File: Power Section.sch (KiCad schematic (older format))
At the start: 55 parts, among them J17 CK-JS102011SAQN, J4 USB_C_Receptacle_USB2.0, Q1 SSM6J507NU, Q2 SSM6J507NU, Q3 SSM6J507NU, U1 LM1117LDX, U2 LDFM33PVR, U5 MCP73213, U6 ETA3000, U7 STUSB4500QTR

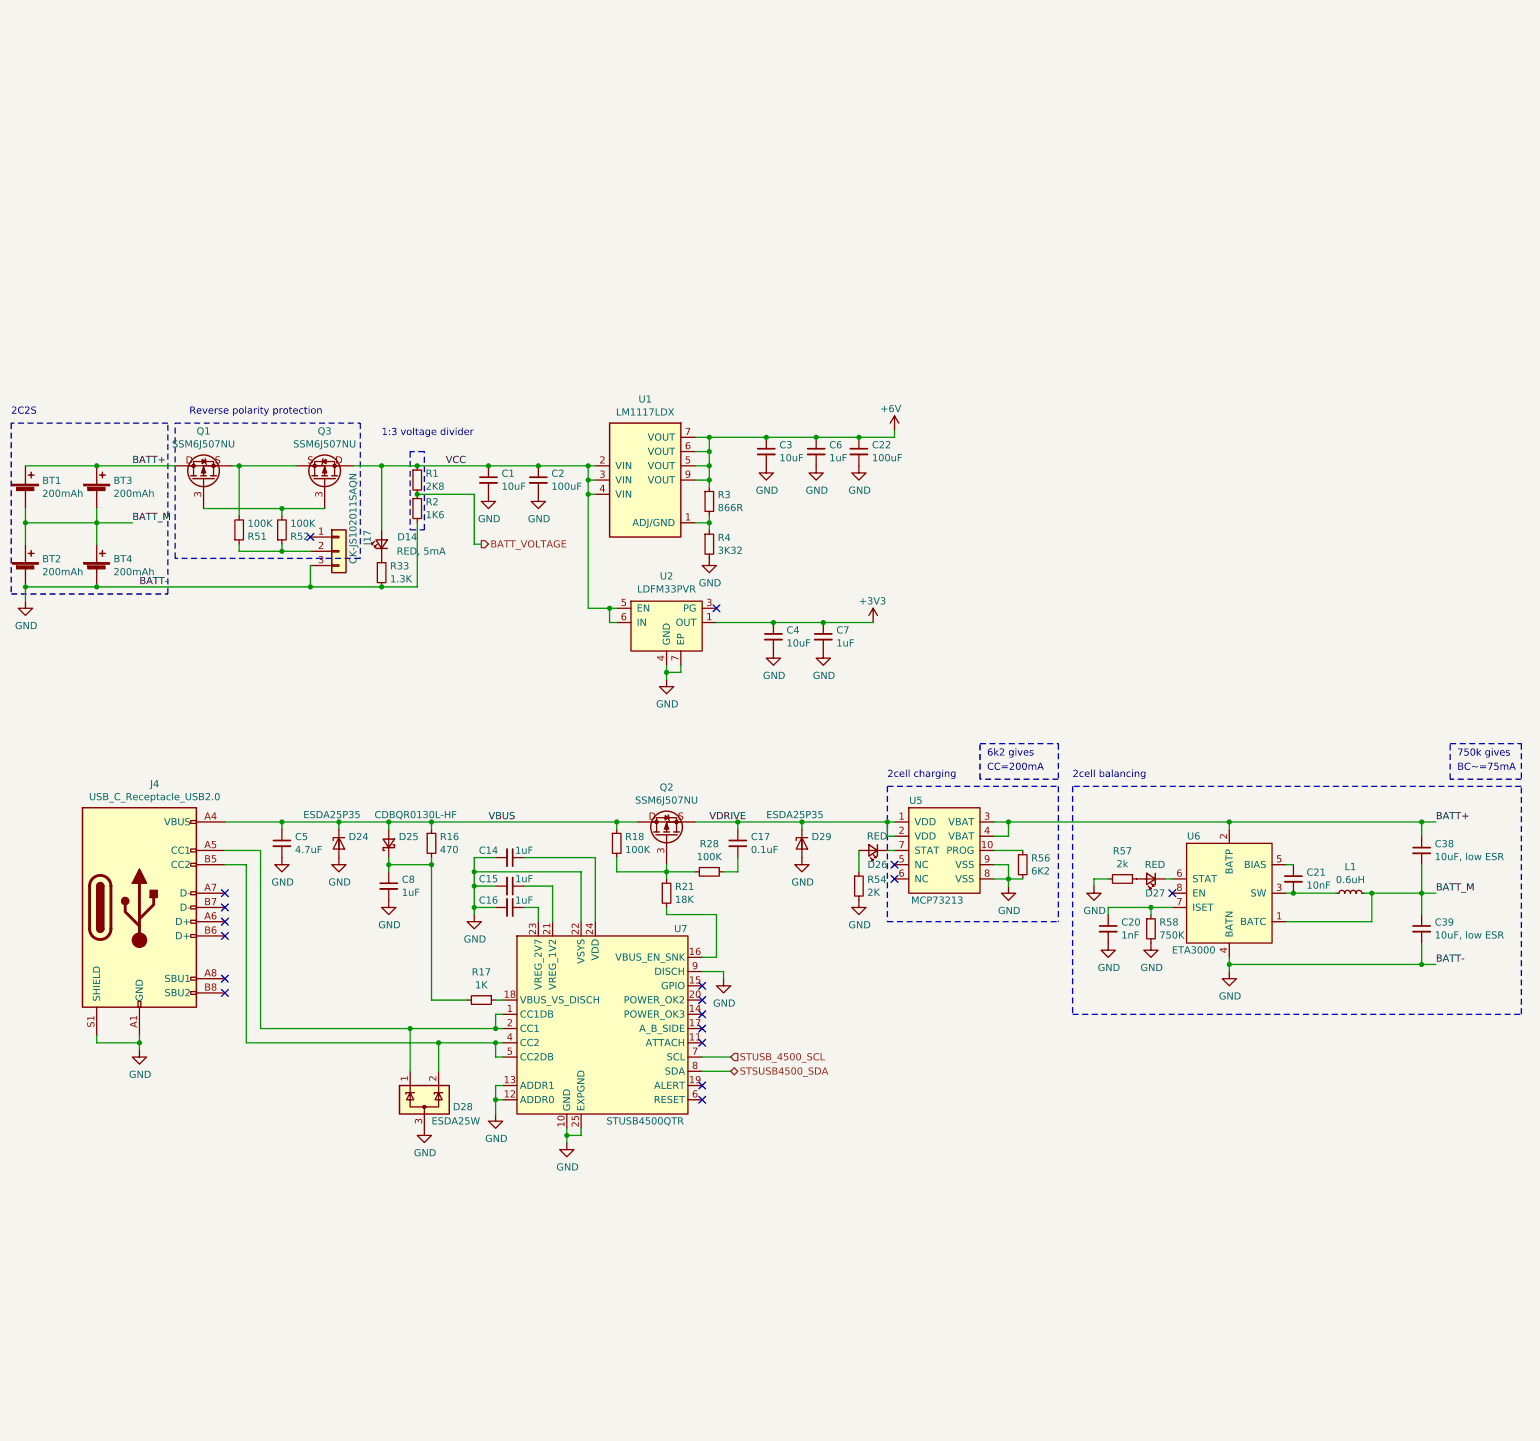
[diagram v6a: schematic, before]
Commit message: Dodano możliwość zasilania (nie tylko ładowania)  myszki z usb-c
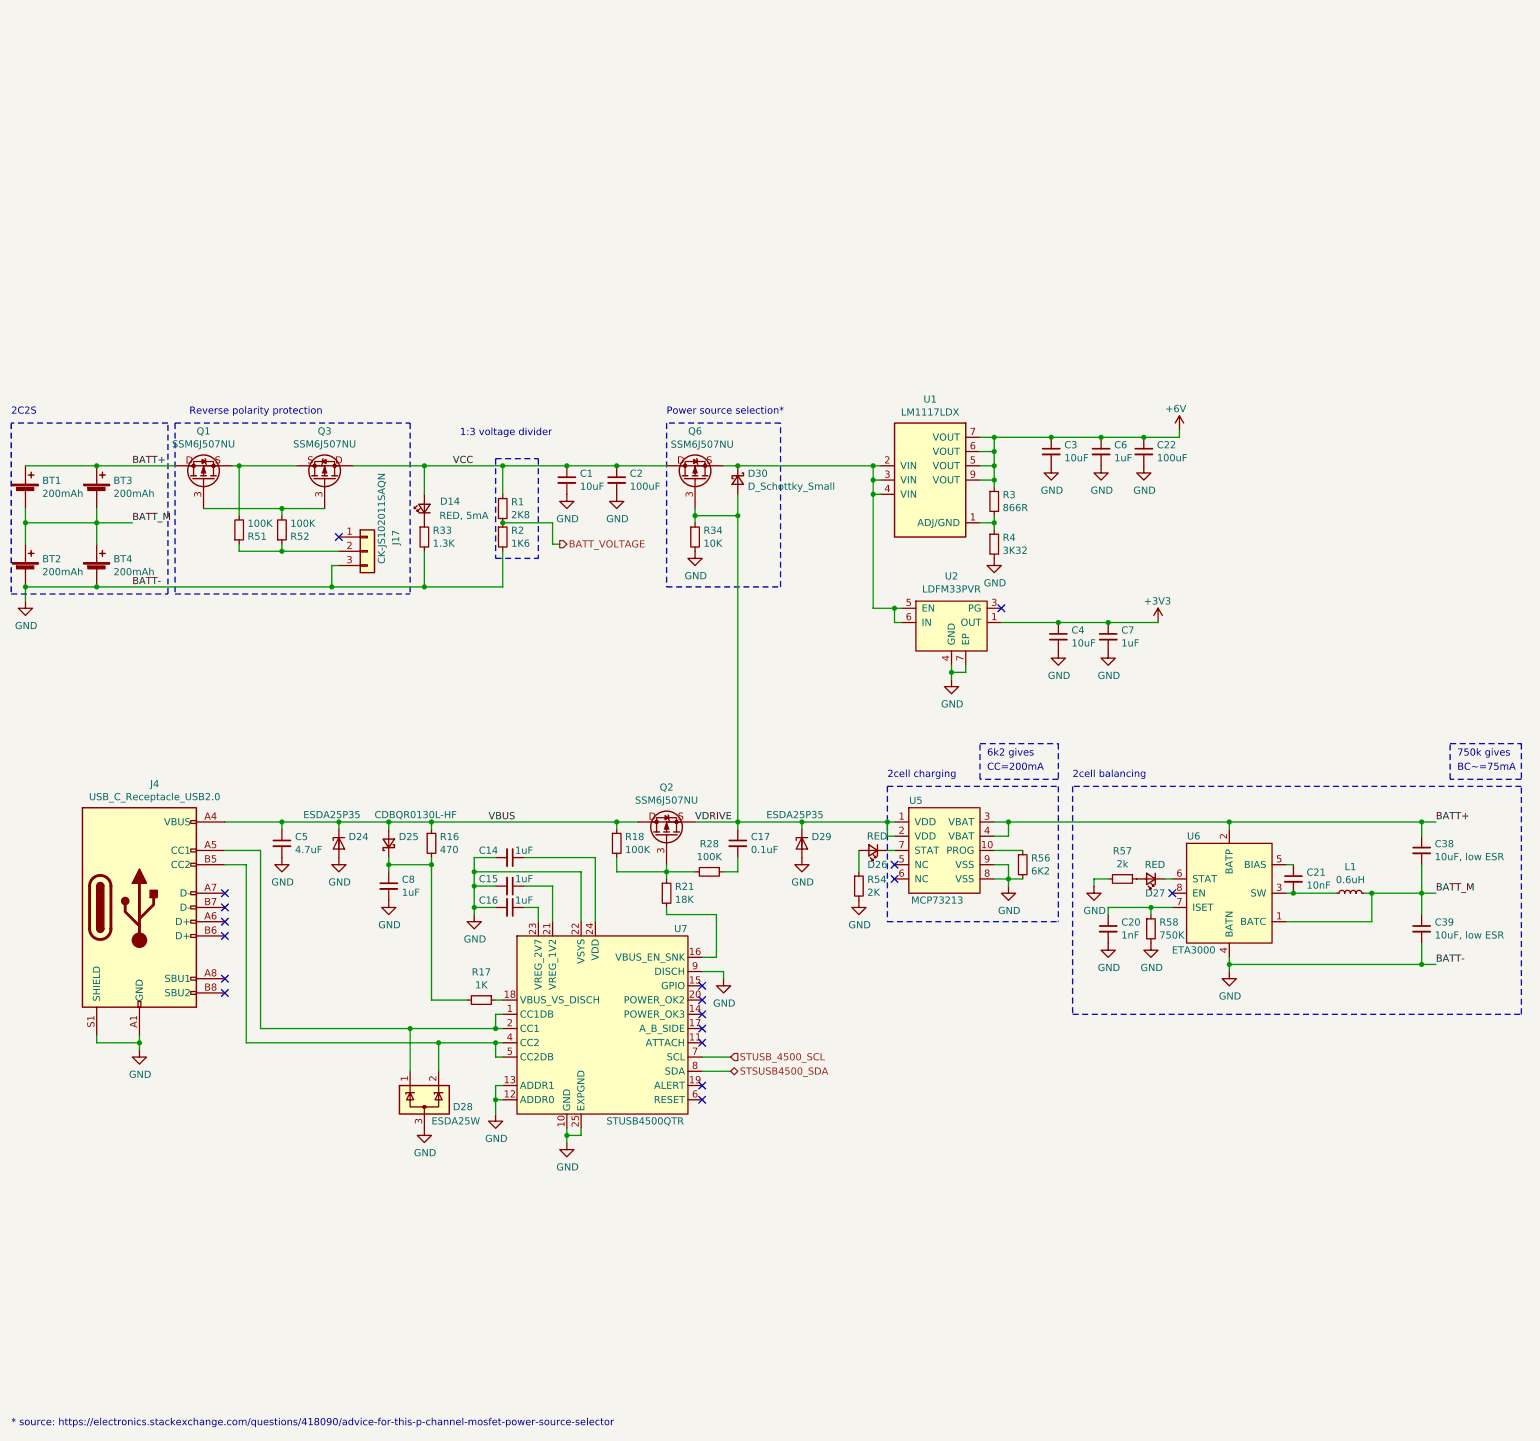
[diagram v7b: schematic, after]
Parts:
- added D30: D_Schottky_Small, symbol Device:D_Schottky_Small
- added Q6: SSM6J507NU, footprints:UDFN6B, symbol synermycha-electronics:SSM6J507NU
- added R34: 10K, Resistor_SMD:R_0402_1005Metric, symbol Device:R_Small
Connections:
- net GND: now also R34.2
- net VCC: now also Q6.1 (D), Q6.2 (D), Q6.5 (D), Q6.6 (D), Q6.D; no longer U1.2 (VIN), U1.3 (VIN), U1.4 (VIN), U2.5 (EN), U2.6 (IN)
- net VDRIVE: now also D30.2 (A), Q6.3 (G), R34.1
- new net: D30.1 (K), Q6.4 (S), Q6.S, U1.2 (VIN), U1.3 (VIN), U1.4 (VIN), U2.5 (EN), U2.6 (IN)
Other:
- note added: "* source: https://electronics.stackexchange.com/questions/418090/advice-for-this-p-channel-mosfet-power-source-selector"
- note added: "Power source selection*"
- moved on the sheet: C1, C2, C22, C3, C4, C6, C7, D14, J17, R1, R2, R3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

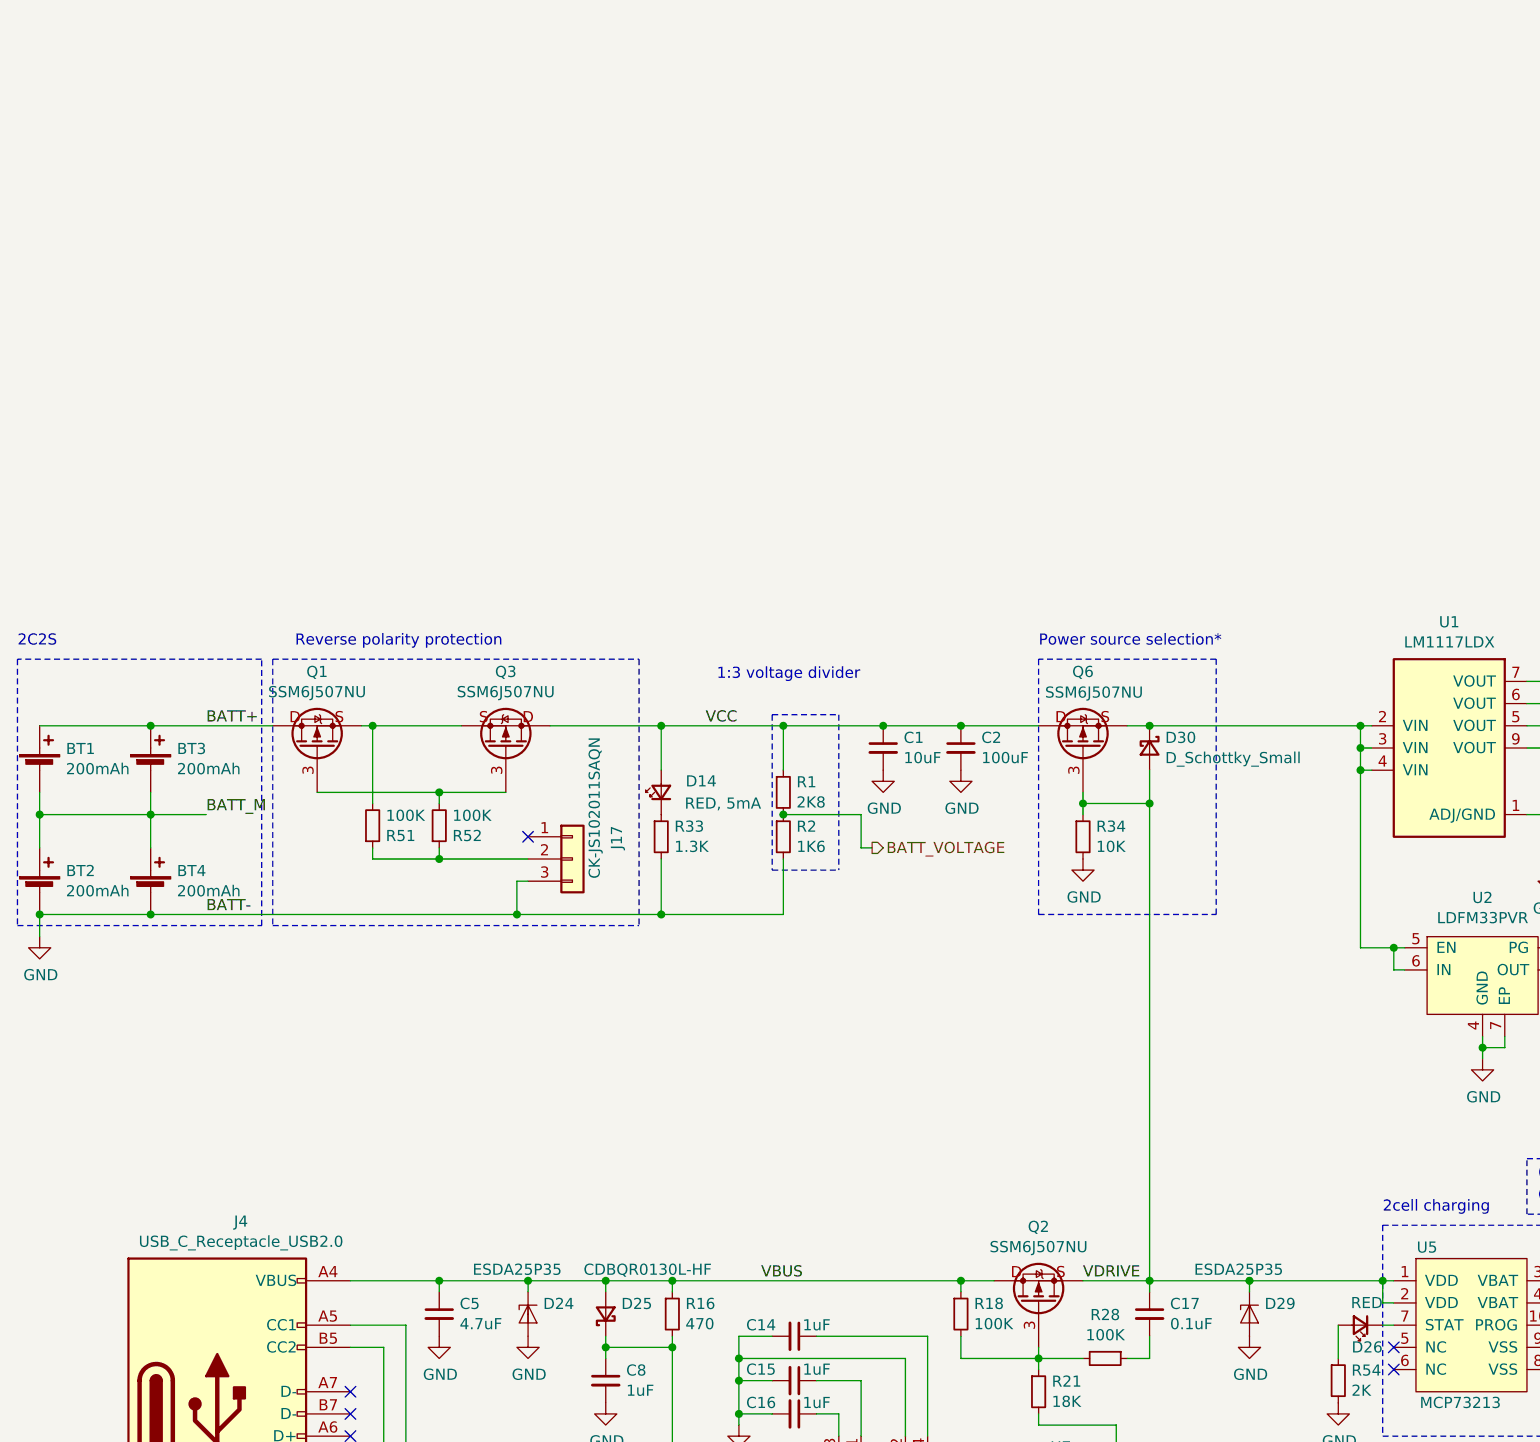
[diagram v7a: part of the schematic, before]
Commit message: Myszka może być wyłączona także podczas zasilania z USB. Zmiany na PCB
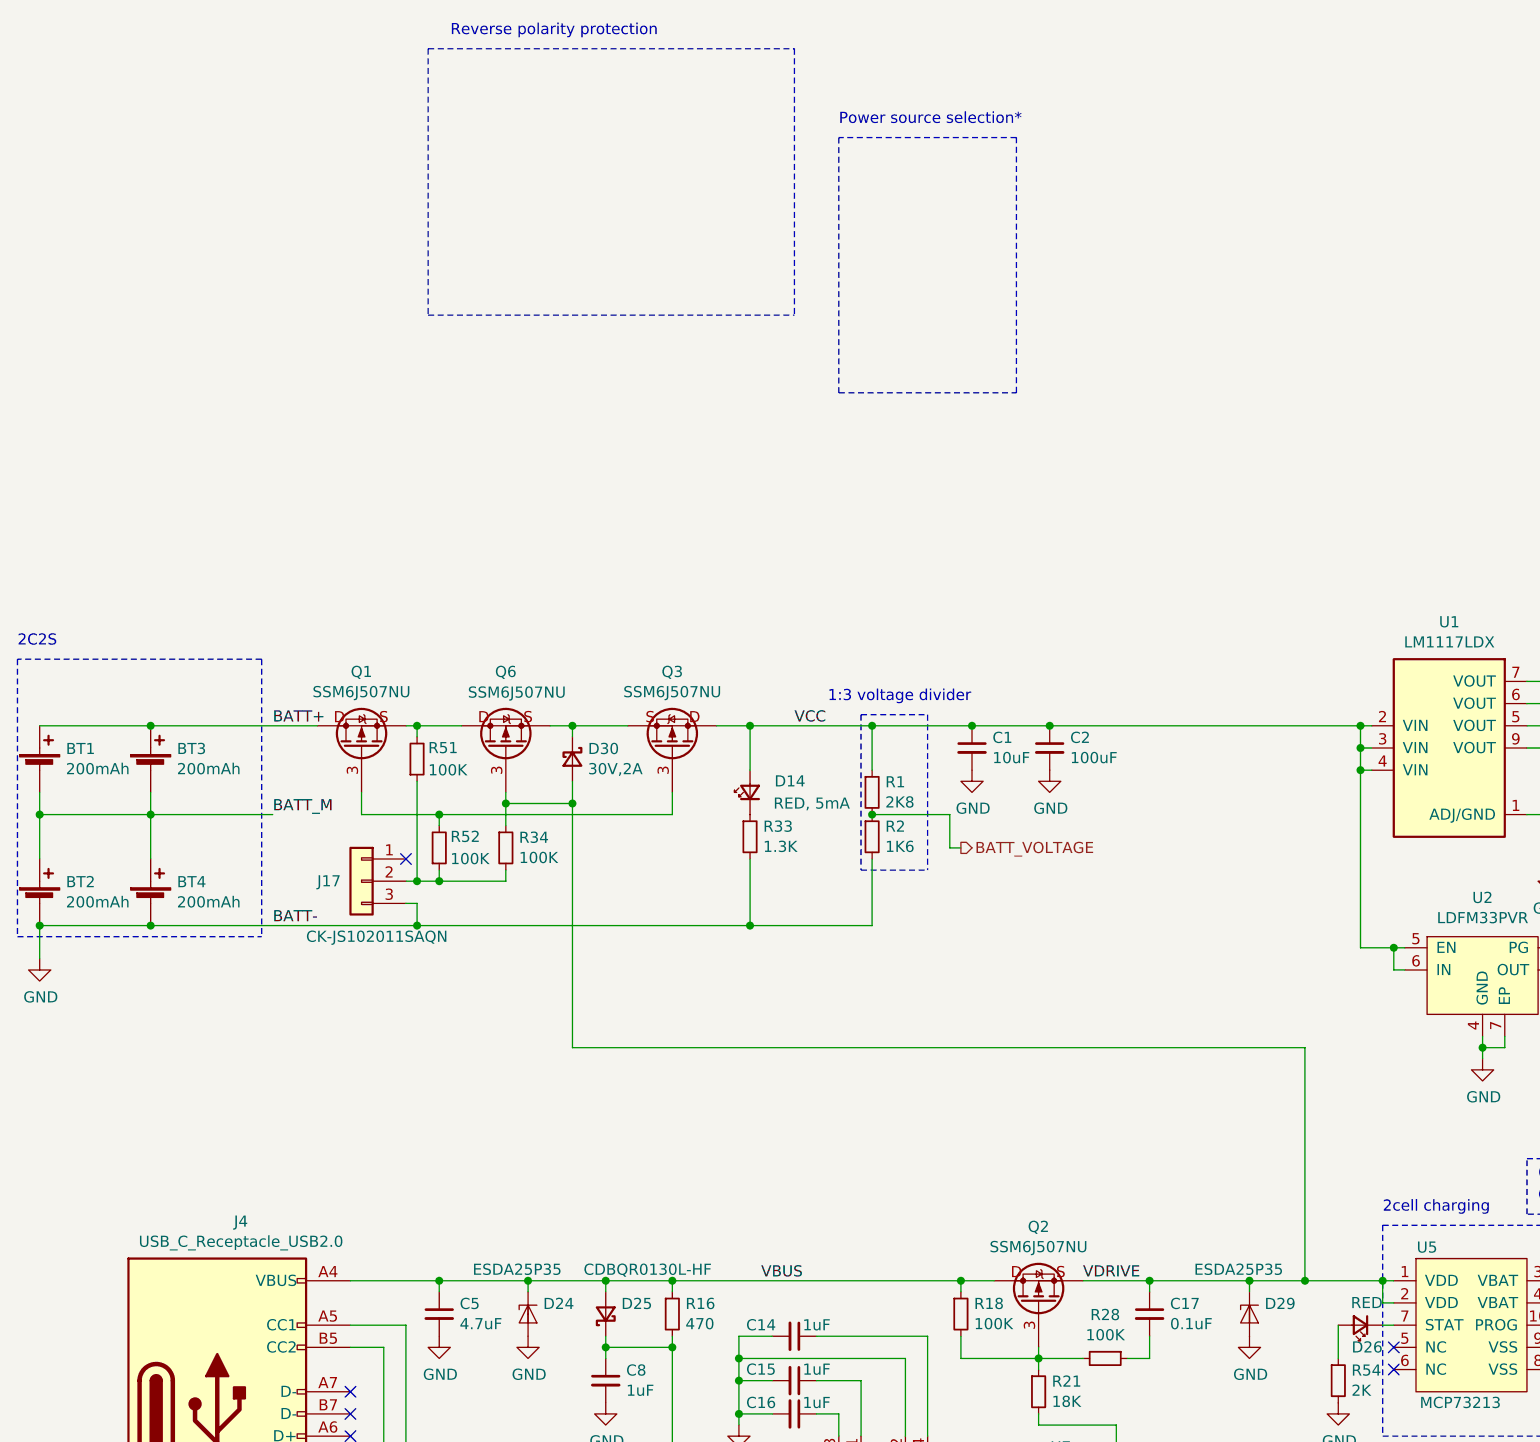
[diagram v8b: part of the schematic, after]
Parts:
- D30: value D_Schottky_Small -> 30V,2A; footprint (none) -> Diode_SMD:D_SOD-123F
- R34: value 10K -> 100K
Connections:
- net GND: no longer R34.2
- net VCC: now also U1.2 (VIN), U1.3 (VIN), U1.4 (VIN), U2.5 (EN), U2.6 (IN); no longer Q6.1 (D), Q6.2 (D), Q6.5 (D), Q6.6 (D), Q6.D
- net at J17.2 (Pin_2), R51.1, R52.1: now also R34.2
- net at Q1.4 (S), Q1.S, R51.2: now also Q6.1 (D), Q6.2 (D), Q6.5 (D), Q6.6 (D), Q6.D; no longer Q3.4 (S), Q3.S
- new net: D30.1 (K), Q3.4 (S), Q3.S, Q6.4 (S), Q6.S
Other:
- moved on the sheet: BT2, BT4, C1, C2, D14, D30, J17, Q1, Q3, Q6, R1, R2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
